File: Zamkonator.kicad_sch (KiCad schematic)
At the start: 9 parts, among them J1 Screw_Terminal_01x06, J3 Conn_01x08_Male, J4 Conn_02x06_Counter_Clockwise

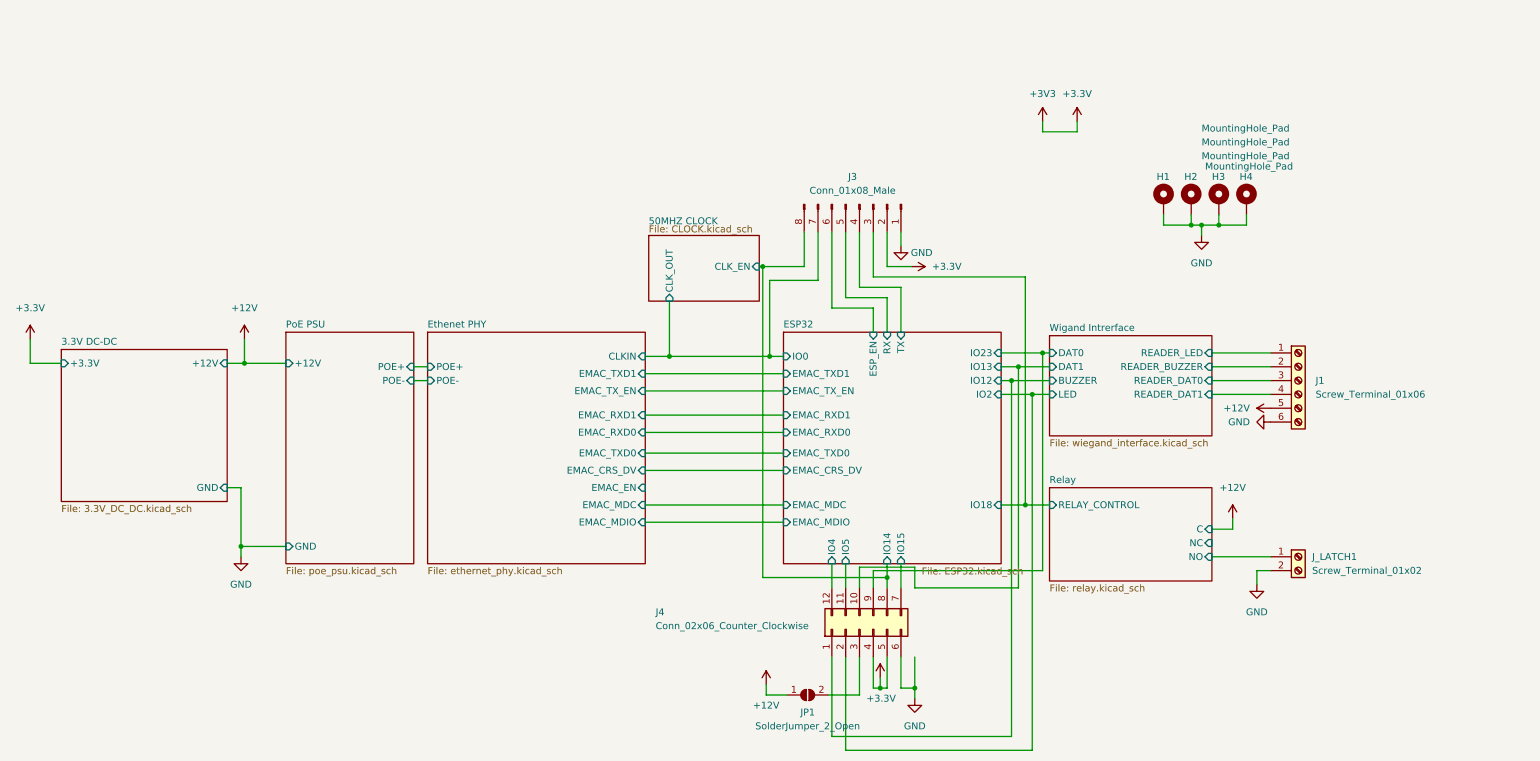
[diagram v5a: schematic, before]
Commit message: Add testpoints, jumpers
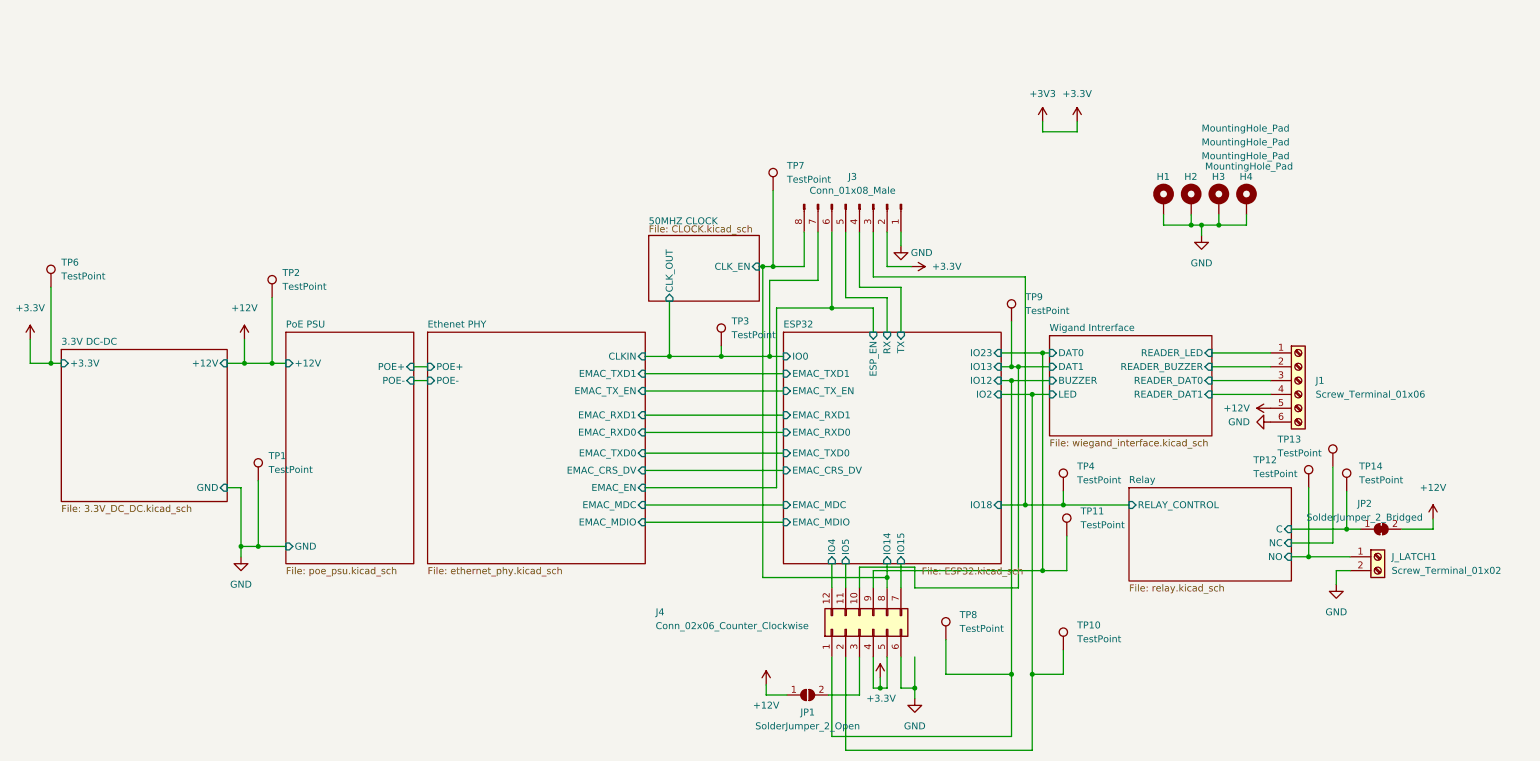
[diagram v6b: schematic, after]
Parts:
- added JP2: SolderJumper_2_Bridged, Jumper:SolderJumper-2_P1.3mm_Bridged_RoundedPad1.0x1.5mm, symbol Jumper:SolderJumper_2_Bridged
- added TP1, TP12, TP13, TP14, TP2, TP6: TestPoint, TestPoint:TestPoint_Pad_D3.0mm, symbol Connector:TestPoint
- added TP10, TP11, TP3, TP4, TP7, TP8, TP9: TestPoint, TestPoint:TestPoint_Pad_D1.5mm, symbol Connector:TestPoint
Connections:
- net +12V: now also JP2.2 (B), TP2.1
- net +3.3V: now also TP6.1
- net 50MHZ CLOCK/CLK_EN: now also TP7.1
- net 50MHZ CLOCK/CLK_OUT: now also TP3.1
- net ESP32/IO12: now also TP8.1
- net ESP32/IO13: now also TP9.1
- net ESP32/IO18: now also TP4.1
- net ESP32/IO2: now also TP10.1
- net ESP32/IO23: now also TP11.1
- net GND: now also TP1.1
- net Relay/NC: now also TP13.1
- net Relay/NO: now also TP12.1
- new net Relay/C: JP2.1 (A), TP14.1
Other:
- moved on the sheet: J_LATCH1

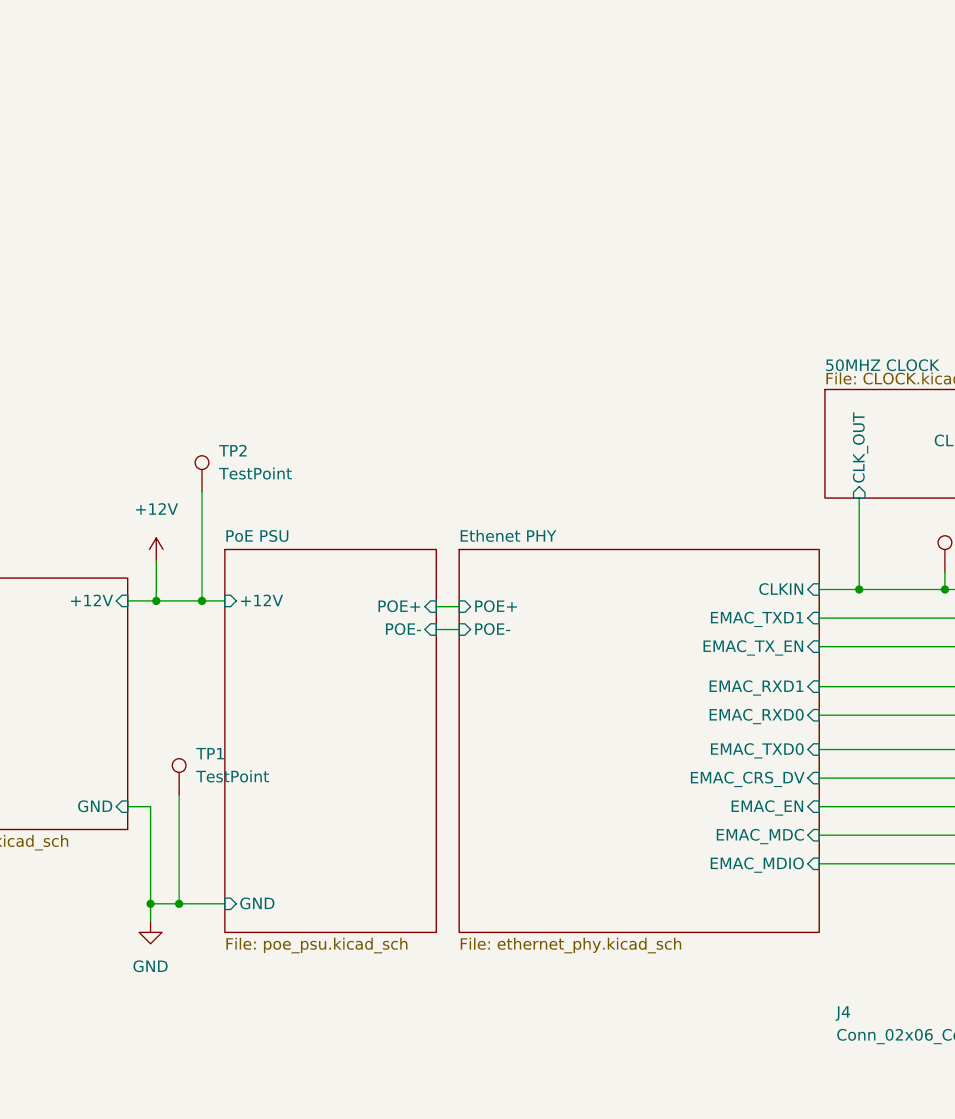
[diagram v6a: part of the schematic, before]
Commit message: RT9400 module option added
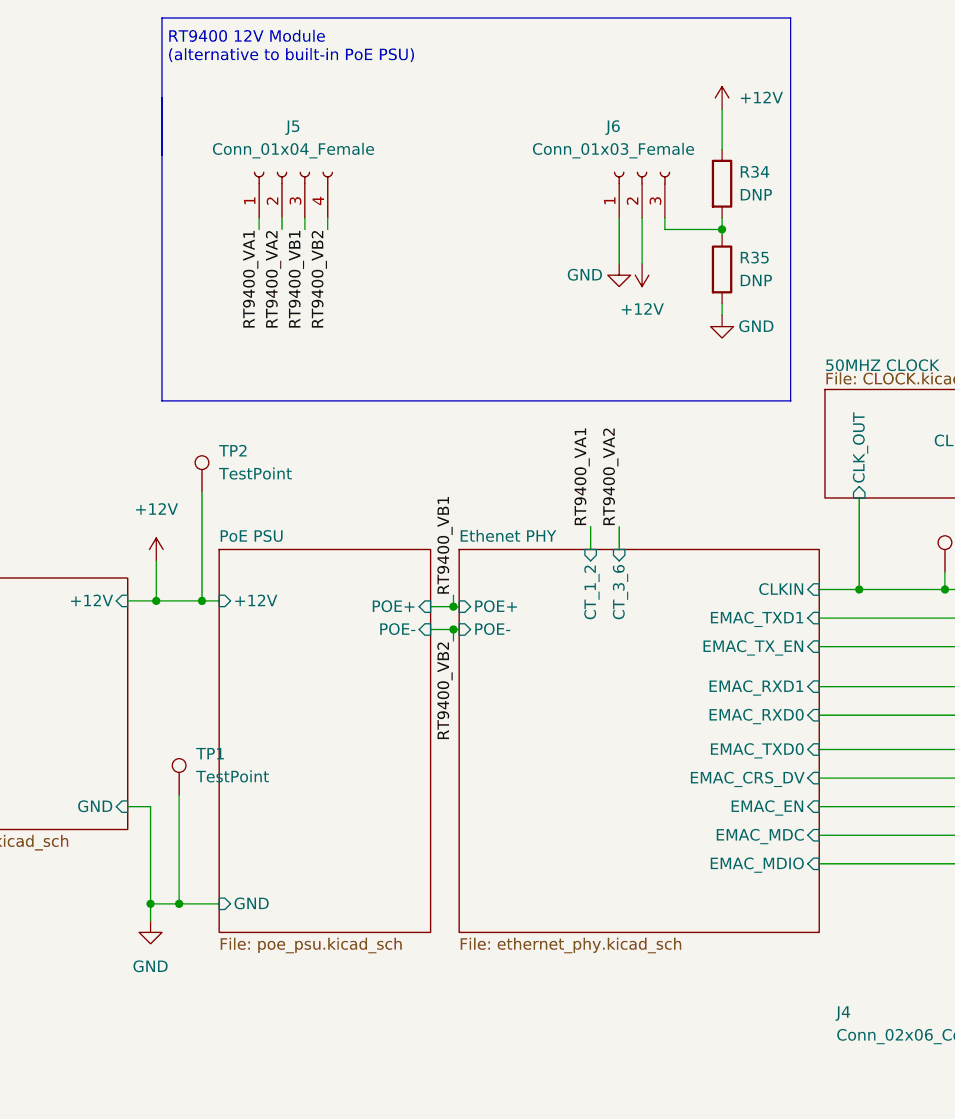
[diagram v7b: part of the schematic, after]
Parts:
- added J5: Conn_01x04_Female, Connector_PinSocket_2.54mm:PinSocket_1x04_P2.54mm_Vertical, symbol Connector:Conn_01x04_Female
- added J6: Conn_01x03_Female, Connector_PinSocket_2.54mm:PinSocket_1x03_P2.54mm_Vertical, symbol Connector:Conn_01x03_Female
- added R34, R35: DNP, Resistor_SMD:R_0603_1608Metric_Pad0.98x0.95mm_HandSolder, symbol Device:R
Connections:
- net +12V: now also J6.2 (Pin_2), R34.1
- net GND: now also J6.1 (Pin_1), R35.2
- new net: J6.3 (Pin_3), R34.2, R35.1
- new net RT9400_VA1: J5.1 (Pin_1)
- new net RT9400_VA2: J5.2 (Pin_2)
- new net RT9400_VB1: J5.3 (Pin_3)
- new net RT9400_VB2: J5.4 (Pin_4)
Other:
- sheet Ethenet PHY ports: added CT_1_2, CT_3_6; removed none
- note added: "RT9400 12V Module (alternative to built-in PoE PSU)"
